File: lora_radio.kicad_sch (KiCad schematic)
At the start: 35 parts, among them J3 ANT, Q9 DMN3731U-7, U10 PE4259, U9 SX1262, Y1 32MHz

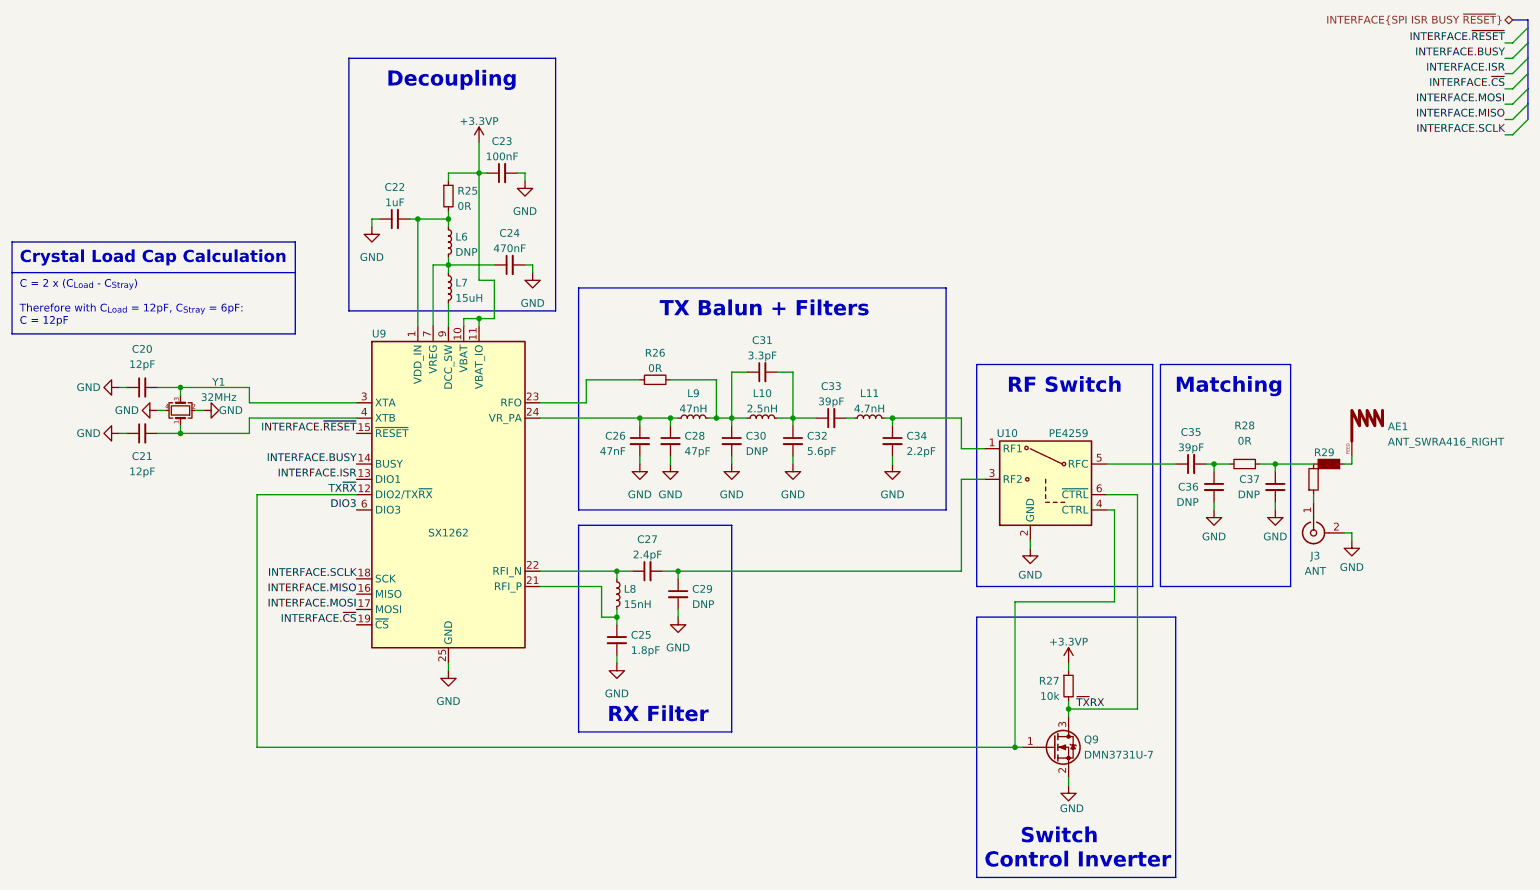
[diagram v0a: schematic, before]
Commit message: Swapped to NRF and made a bunch of progress
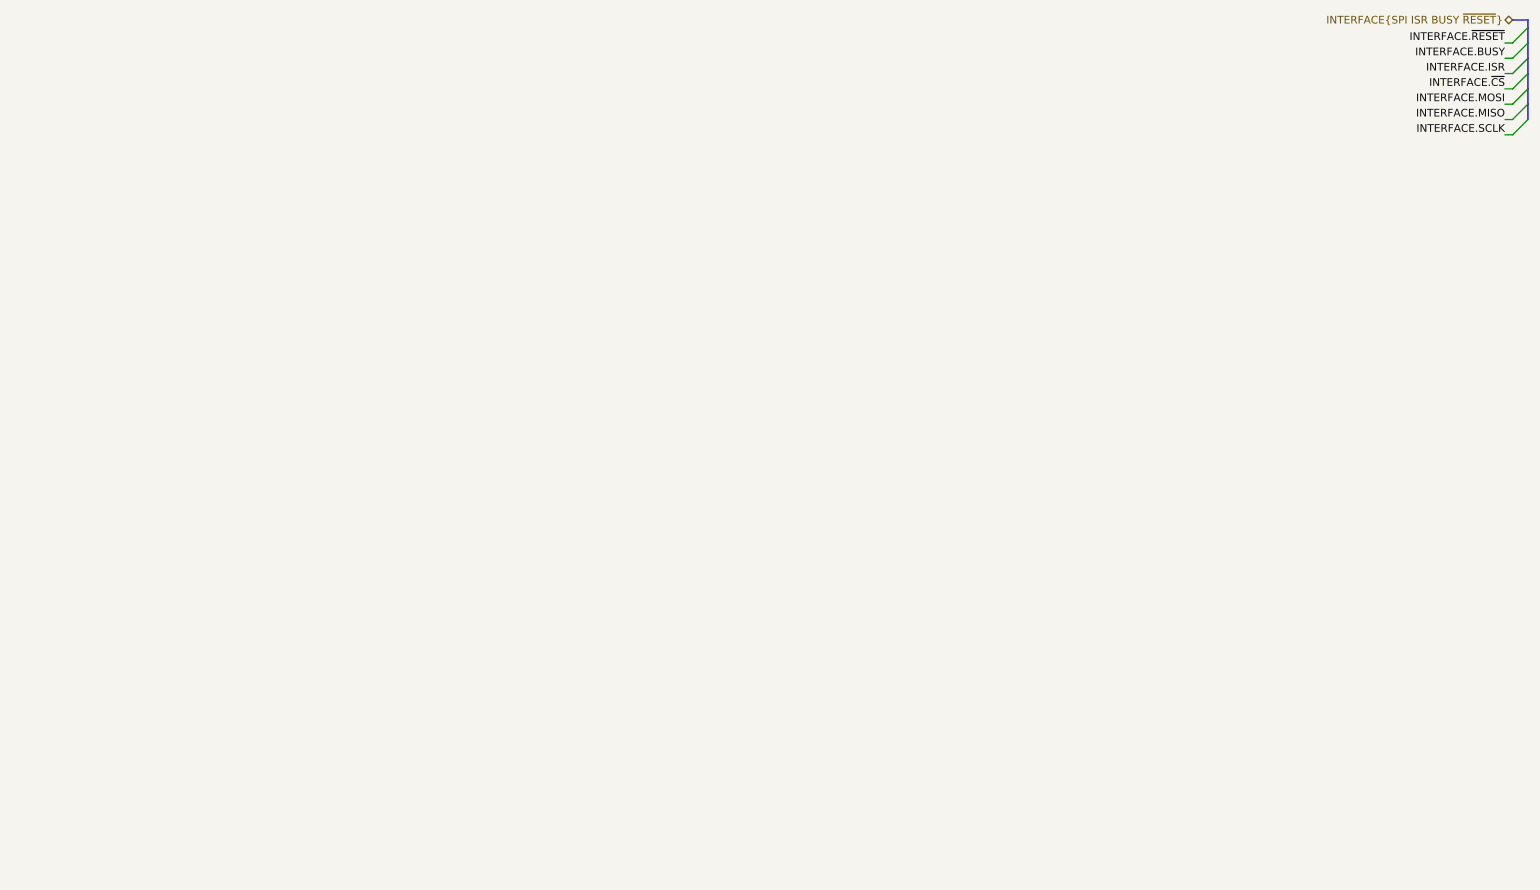
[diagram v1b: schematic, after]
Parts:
- removed AE1: ANT_SWRA416_RIGHT, plentify_footprints:SWRA416_RIGHT, symbol plentify_symbols:ANT_SWRA416_RIGHT
- removed C20, C21: 12pF, plentify_footprints:CAPACITOR_0402, symbol plentify_symbols:CAP_0402_12pF_6.3v_C0G
- removed C22: 1uF, plentify_footprints:CAPACITOR_0402, symbol plentify_symbols:CAP_0402_1uF_6.3v_X7R
- removed C23: 100nF, plentify_footprints:CAPACITOR_0402, symbol plentify_symbols:CAP_0402_100nF_6.3v_X7R
- removed C24: 470nF, plentify_footprints:CAPACITOR_0402, symbol plentify_symbols:CAP_0402_470nF_6.3v_X7R
- removed C25: 1.8pF, plentify_footprints:CAPACITOR_0402, symbol plentify_symbols:CAP_0402_1.8pF_6.3v_C0G
- removed C26: 47nF, plentify_footprints:CAPACITOR_0402, symbol plentify_symbols:CAP_0402_47nF_6.3v_C0G
- removed C27: 2.4pF, plentify_footprints:CAPACITOR_0402, symbol plentify_symbols:CAP_0402_2.4pF_6.3v_C0G
- removed C28: 47pF, plentify_footprints:CAPACITOR_0402, symbol plentify_symbols:CAP_0402_47pF_6.3v_C0G
- removed C29, C30, C36, C37: DNP, plentify_footprints:CAPACITOR_0402_DNP, symbol plentify_symbols:CAP_0402_DNP
- removed C31: 3.3pF, plentify_footprints:CAPACITOR_0402, symbol plentify_symbols:CAP_0402_3.3pF_6.3v_C0G
- removed C32: 5.6pF, plentify_footprints:CAPACITOR_0402, symbol plentify_symbols:CAP_0402_5.6pF_6.3v_C0G
- removed C33, C35: 39pF, plentify_footprints:CAPACITOR_0402, symbol plentify_symbols:CAP_0402_39pF_6.3v_C0G
- removed C34: 2.2pF, plentify_footprints:CAPACITOR_0402, symbol plentify_symbols:CAP_0402_2.2pF_6.3v_C0G
- removed J3: ANT, plentify_footprints:U.FL_CONNECTOR, symbol plentify_symbols:u.FL_CONNECTOR
- removed L10: 2.5nH, plentify_footprints:INDUCTOR_0402, symbol plentify_symbols:IND_0402_2.5nH
- removed L11: 4.7nH, plentify_footprints:INDUCTOR_0402, symbol plentify_symbols:IND_0402_4.7nH
- removed L6: DNP, plentify_footprints:INDUCTOR_0402_DNP, symbol plentify_symbols:IND_0402_DNP
- removed L7: 15uH, plentify_footprints:INDUCTOR_0603, symbol plentify_symbols:IND_0603_15uH
- removed L8: 15nH, plentify_footprints:INDUCTOR_0402, symbol plentify_symbols:IND_0402_15nH
- removed L9: 47nH, plentify_footprints:INDUCTOR_0402, symbol plentify_symbols:IND_0402_47nH
- removed Q9: DMN3731U-7, plentify_footprints:SOT-23, symbol plentify_symbols:DMN3731U-7
- removed R25, R26, R28: 0R, plentify_footprints:RESISTOR_0402, symbol plentify_symbols:RES_0402_0R_5%
- removed R27: 10k, plentify_footprints:RESISTOR_0402, symbol plentify_symbols:RES_0402_10k_1%
- removed R29: RES_0402_0R_SELECTOR_LEFT, plentify_footprints:RESISTOR_0402_SELECTOR_LEFT, symbol plentify_symbols:RES_0402_0R_SELECTOR_LEFT
- removed U10: PE4259, plentify_footprints:SOT-363_SC-70-6, symbol plentify_symbols:PE4259
- removed U9: SX1262, plentify_footprints:QFN-24-1EP_4x4mm_P0.5mm_EP2.7x2.7mm, symbol plentify_symbols:SX1262
- removed Y1: 32MHz, plentify_footprints:CRYSTAL_3225, symbol plentify_symbols:CRYSTAL_32MHz_12pF
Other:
- note removed: "C = 2 x (C_{Load} - C_{Stray}) Therefore with C_{Load} = 12pF, C_{Stray} = 6pF: C = 12pF"
- note removed: "Crystal Load Cap Calculation"
- note removed: "Decoupling"
- note removed: "Matching"
- note removed: "RF Switch"
- note removed: "RX Filter"
- note removed: "Switch Control Inverter"
- note removed: "TX Balun + Filters"
